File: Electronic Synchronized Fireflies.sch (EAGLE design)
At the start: 20 parts, among them IC1 NCP1400A, IC2 G2X[2/3]1---PW14, X1 22-23-2121, X2 22-23-2121

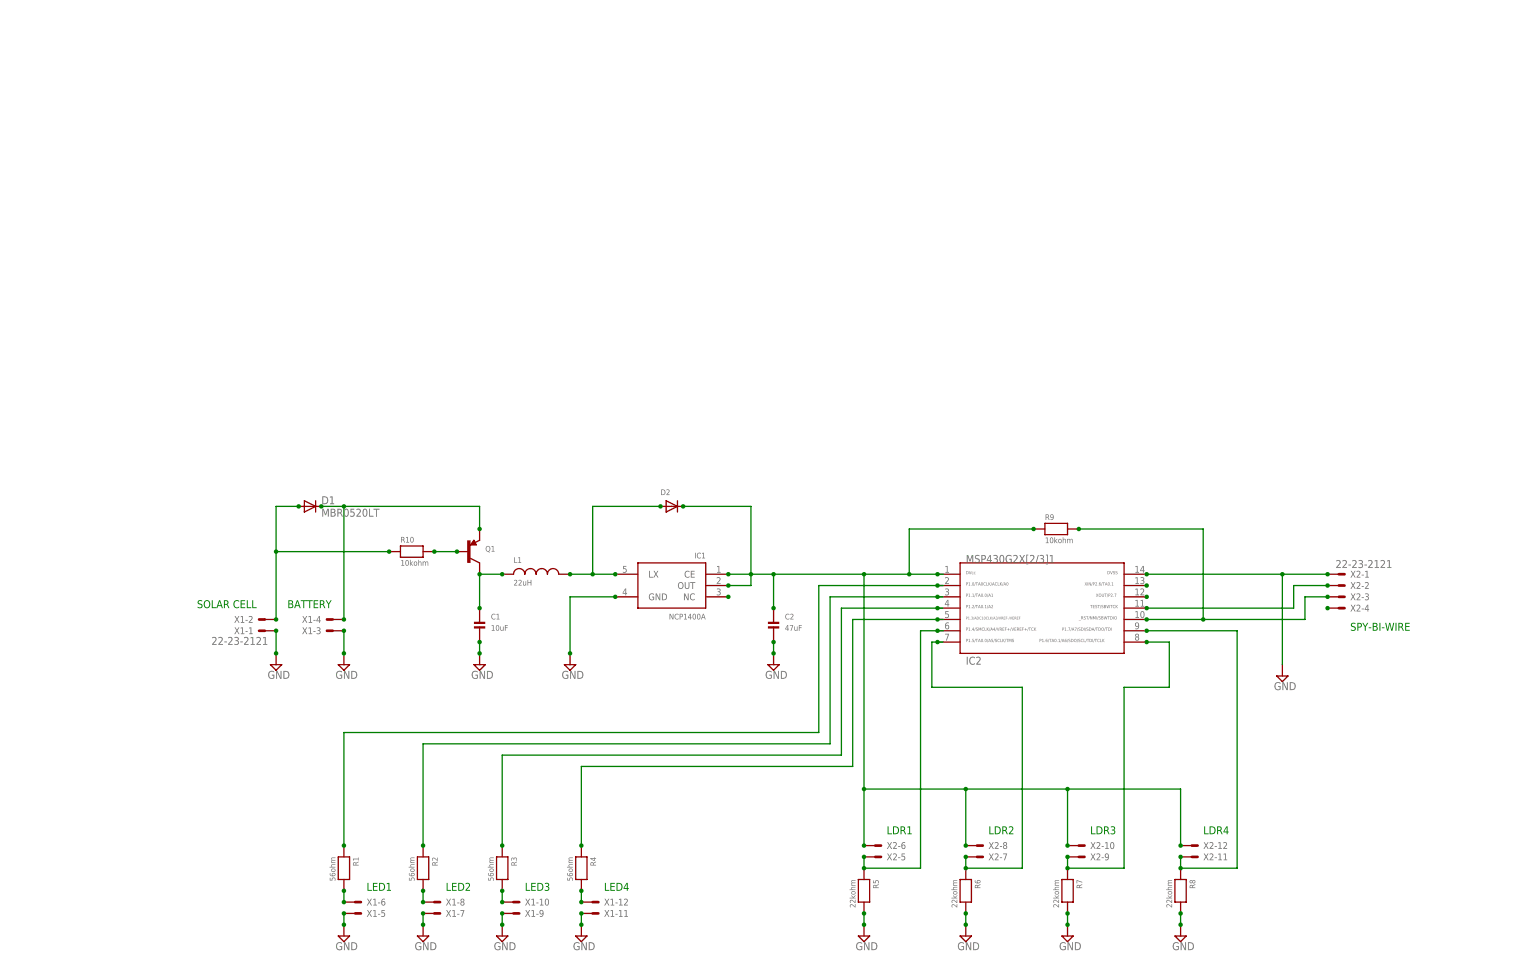
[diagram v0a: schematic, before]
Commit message: Added power control, PCB improvements
v0.2
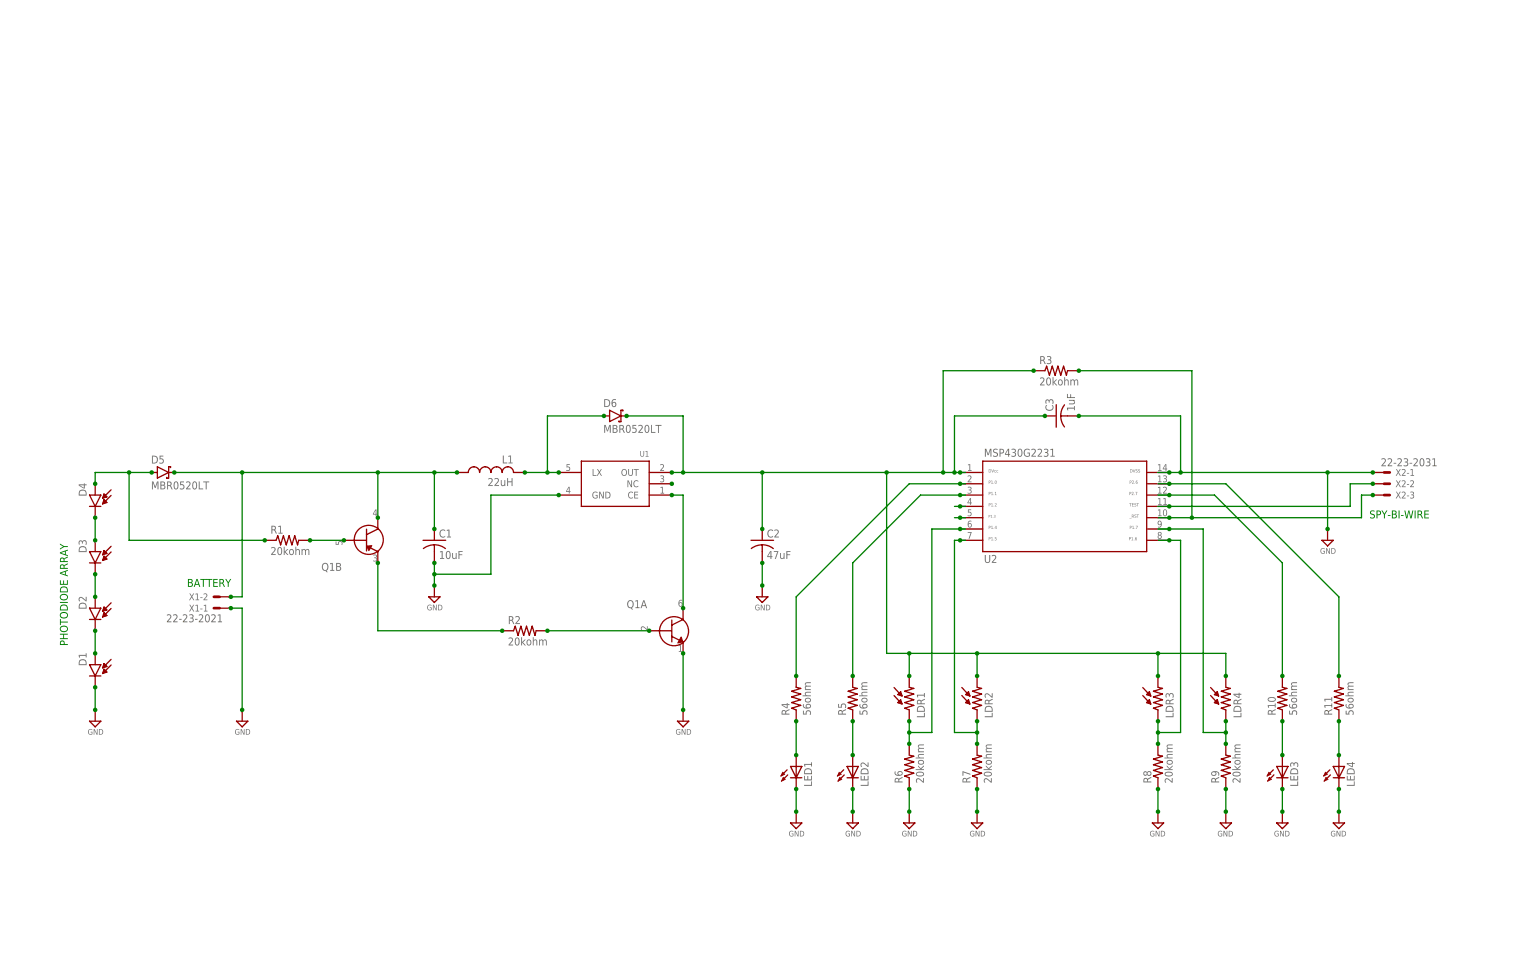
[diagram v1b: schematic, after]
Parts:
- removed IC1: NCP1400A, microbuilder:NCP1400A_STEPUP
- removed IC2: G2X[2/3]1---PW14, TI_MSP430_v16:G2X[2/3]1---PW14
- added C3: 1uF, Firefly:CAPACITORC0805
- added D3, D4: PHOTODIODESMD2, Firefly:PHOTODIODESMD2
- added D5, D6: MBR0520LT, Firefly:MBR0520LT
- added LDR1, LDR2, LDR3, LDR4: LDR, Firefly:LDR
- added LED1, LED2, LED3, LED4: (no value), Firefly:LED5MM
- added R11: 56ohm, Firefly:RESISTORSR0805
- added U1: (no value), Firefly:NCP1400A
- added U2: MSP430G2231/TSSOP-14, Firefly:MSP430G2231/TSSOP-14
- C1, C2: device microbuilder:CAP_CERAMIC0805 -> Firefly:CAPACITORC0805
- D1: value MBR0520LT -> PHOTODIODESMD2; device diode:MBR0520LT -> Firefly:PHOTODIODESMD2
- D2: value (none) -> PHOTODIODESMD2; device microbuilder:DIODESMA -> Firefly:PHOTODIODESMD2
- L1: device microbuilder:INDUCTOR0805 -> Firefly:L-US
- Q1: value (none) -> NPN/PNP; device microbuilder:TRANSISTOR_PNPSOT23-REFLOW -> Firefly:NPN/PNP
- R1, R2, R3: value 56ohm -> 20kohm; device microbuilder:RESISTOR0805 -> Firefly:RESISTORSR0805
- R10: value 10kohm -> 56ohm; device microbuilder:RESISTOR0805 -> Firefly:RESISTORSR0805; PARTNUMBER ERJ-8GEYJ222V -> (none)
- R4: device microbuilder:RESISTOR0805 -> Firefly:RESISTORSR0805
- R5: value 22kohm -> 56ohm; device microbuilder:RESISTOR0805 -> Firefly:RESISTORSR0805
- R6, R7, R8: value 22kohm -> 20kohm; device microbuilder:RESISTOR0805 -> Firefly:RESISTORSR0805
- R9: value 10kohm -> 20kohm; device microbuilder:RESISTOR0805 -> Firefly:RESISTORSR0805
- X1: value 22-23-2121 -> 22-23-2021; device con-molex:22-23-2121 -> Firefly:22-23-2021
- X2: value 22-23-2121 -> 22-23-2031; device con-molex:22-23-2121 -> Firefly:22-23-2031
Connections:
- new net N$29: LDR3.1, R8.2, U2.8
- new net N$30: LDR4.1, R9.2, U2.9
- new net N$31: LED3.A, R10.1
- new net N$32: LED4.A, R11.1
- net GND: now also C1.2, C2.2, C3.2, D1.C, LED1.C, LED2.C, LED3.C, LED4.C, Q1A.E, R6.1, R7.1, R8.1, R9.1, U1.GND, U2.14; no longer C1.P$2, C2.P$2, IC1.GND, IC2.14, R5.2, R6.2, R7.2, R8.2, X1-11.S, X1-3.S, X1-5.S, X1-7.S, X1-9.S
- net N$1: now also D2.C; no longer R10.1, X1-2.S
- net N$10: now also Q1A.C, U1.CE; no longer R2.2, X1-8.S
- net N$11: now also R4.2, U2.2; no longer R3.2, X1-10.S
- net N$12: now also R5.2, U2.3; no longer R4.2, X1-12.S
- net N$13: now also U2.4; no longer IC2.6, R5.1, X2-5.S
- net N$14: now also R3.2, U2.10, X2-3.S; no longer IC2.13
- net N$15: now also U2.5; no longer IC2.7, R6.1, X2-7.S
- net N$16: now also LDR2.1, R7.2, U2.7; no longer IC2.8, R7.1, X2-9.S
- net N$17: now also LDR1.1, R6.2, U2.6; no longer IC2.9, R8.1, X2-11.S
- net N$18: now also LED2.A, R5.1; no longer IC2.11, X2-2.S
- net N$19: now also D3.A, D4.C; no longer IC2.10, R9.2, X2-3.S
- net N$2: now also Q1B.B, R1.2; no longer D1.C, Q1.E, X1-4.S
- net N$20: now also U2.11, X2-2.S; no longer IC2.12
- net N$21: now also R11.2, U2.13; no longer X2-4.S
- net N$22: now also D4.A, D5.A, R1.1; no longer IC1.NC
- net N$23: now also R10.2, U2.12; no longer C1.P$1, L1.1, Q1.C
- net N$24: now also LED1.A, R4.1; no longer Q1.B, R10.2
- net N$3: now also D3.C; no longer IC1.LX, L1.2
- net N$4: now also C1.1, D5.C, L1.1, Q1B.C, X1-2.S; no longer IC2.3, R2.1
- net N$5: now also D6.A, L1.2, U1.LX; no longer C2.P$1, D2.C, IC1.CE, IC1.OUT, IC2.1, R9.1, X2-10.S, X2-12.S, X2-6.S, X2-8.S
- net N$6: now also Q1B.E, R2.1; no longer IC2.2, R1.1
- net N$7: now also U1.NC; no longer IC2.4, R3.1
- net N$8: now also C2.1, C3.1, D6.C, LDR1.2, LDR2.2, LDR3.2, LDR4.2, R3.1, U1.OUT, U2.1; no longer IC2.5, R4.1
- net N$9: now also Q1A.B, R2.2; no longer R1.2, X1-6.S
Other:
- note added: "PHOTODIODE ARRAY"
- note removed: "LDR1"
- note removed: "LDR2"
- note removed: "LDR3"
- note removed: "LDR4"
- note removed: "LED1"
- note removed: "LED2"
- note removed: "LED3"
- note removed: "LED4"
- note removed: "SOLAR CELL"
- moved on the sheet: C1, C2, L1, X1-1, X1-2, X2-1, X2-2, X2-3

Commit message: Connections for panel, battery, PCB improvements
v0.3 EECS 399 Spring 2012
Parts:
- removed D1, D2, D3, D4: PHOTODIODESMD2, Firefly:PHOTODIODESMD2
- added Q2: DMP2035U-7, Firefly:BSS84
- added R12: 20kohm, Firefly:RESISTORSR0805
- added R13, R14, R15, R16, R17: 0ohm, Firefly:RESISTORSR0805
- added TP1, TP2, TP3, TP4, TP5: TPTP08SQ, Firefly:TPTP08SQ
- added X3: 22-23-2021, Firefly:22-23-2021
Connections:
- new net N$25: R11.2, R17.1
- new net N$26: R10.2, R16.1
- net GND: now also TP2.TP, X3-1.S; no longer D1.C
- net N$1: now also LDR1.2, LDR2.2, LDR3.2, LDR4.2, Q2.D; no longer D1.A, D2.C
- net N$11: now also R14.2; no longer R4.2
- net N$12: now also R15.2; no longer R5.2
- net N$13: now also D5.A, R1.1, TP3.TP, X3-2.S
- net N$15: now also Q2.S, R12.1, R13.1; no longer U2.5
- net N$19: now also R14.1, R4.2; no longer D3.A, D4.C
- net N$21: now also R17.2; no longer R11.2
- net N$22: now also R15.1, R5.2; no longer D4.A, D5.A, R1.1
- net N$23: now also R16.2; no longer R10.2
- net N$3: now also Q2.G, R12.2, TP5.TP, U2.5; no longer D2.A, D3.C
- net N$4: now also Q1B.E, TP4.TP; no longer Q1B.C
- net N$6: now also Q1B.C; no longer Q1B.E
- net N$8: now also R13.2, TP1.TP; no longer LDR1.2, LDR2.2, LDR3.2, LDR4.2
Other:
- note added: "SOLAR CELL"
- note removed: "PHOTODIODE ARRAY"
- moved on the sheet: LDR1, LDR2, LDR3, LDR4, LED1, LED2, LED3, LED4, Q1B, R10, R11, R4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

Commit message: Added test points, MOSFET switch, 0R resistors.
v1.0 First run PCB
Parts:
- removed R17: 0ohm, Firefly:RESISTORSR0805
- Q1: value NPN/PNP -> NPN; device Firefly:NPN/PNP -> Firefly:NPN
- R11, R5: value 56ohm -> 20kohm
- R12: value 20kohm -> 0ohm
- R3, R9: value 20kohm -> 56ohm
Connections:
- removed net N$22 (its old number): R15.1, R5.2
- removed net N$25 (its old number): R11.2, R17.1
- removed net N$6: Q1B.C, R2.1
- removed net N$9: Q1A.B, R2.2
- new net N$19: R13.1, R3.2
- new net N$26: R15.1, R9.2
- net GND: now also Q1.E, R5.1; no longer Q1A.E, R9.1
- net N$10: now also Q1.C; no longer Q1A.C
- net N$11: now also R13.2; no longer R14.2
- net N$12: now also R14.2; no longer R15.2
- net N$14: now also R2.2; no longer R3.2
- net N$15: now also R11.1; no longer R13.1
- net N$16: now also R6.2; no longer R7.2
- net N$17: now also R5.2; no longer R6.2
- net N$18: now also R4.1; no longer R5.1
- net N$2: now also Q1.B; no longer Q1B.B
- net N$21: now also R16.2; no longer R17.2
- net N$23: now also R15.2; no longer R16.2
- net N$24: now also R3.1; no longer R4.1
- net N$29: now also R7.2; no longer R8.2
- net N$3: now also R11.2; no longer R12.2
- net N$30: now also R8.2; no longer R9.2
- net N$31: now also R9.1; no longer R10.1
- net N$32: now also R10.1; no longer R11.1
- net N$4: no longer Q1B.E
- net N$8: now also R12.2, R2.1; no longer R13.2, R3.1
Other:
- moved on the sheet: C2, R10, R11, R12, R13, R14, R15, R16, R2, R3, R4, R5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
